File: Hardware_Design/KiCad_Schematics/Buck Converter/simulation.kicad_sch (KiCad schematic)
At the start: 8 parts, among them Q2 PMOS

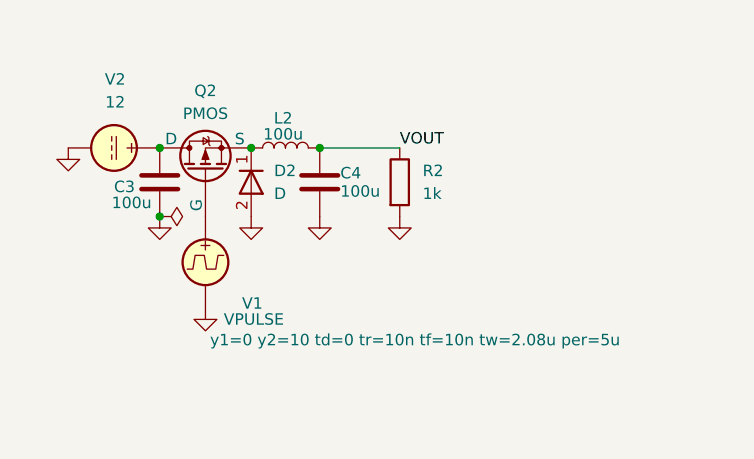
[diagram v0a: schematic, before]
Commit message: init: initialize new circuit for the previous problem
Started the Bootstrap Driver circuit to solve the previous problem. This way, the NMOSFET will be able to operate in full saturation.
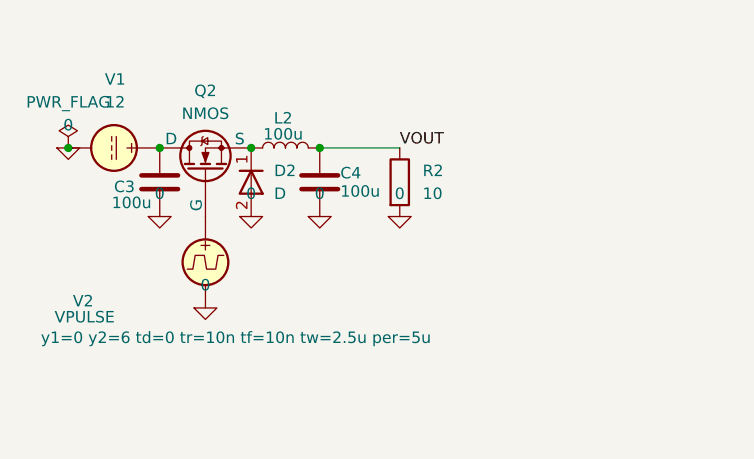
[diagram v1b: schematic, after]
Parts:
- removed Q2: PMOS, symbol Simulation_SPICE:PMOS
- added Q2: NMOS, symbol Simulation_SPICE:NMOS
- R2: value 1k -> 10
- renumbered V2 to V1, V1 to V2
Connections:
- net at C3.1, V1.1: now also Q2.1 (D)
- net at V2.1: now also Q2.2 (G)
- net at D2.1 (K), L2.1: now also Q2.3 (S)
- net GND renamed 0

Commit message: Update designs but continue problems...
Added a Bootstrap circuit to bring the MOSFET from a Linear Regulator state to a Buck Converter state, but the problem is still not resolved. While it should yield a value close to 6V when the Duty Cycle is at 50% and a 12V input is applied, it yields 4V, and the graph is not correct. Work on the problem will continue.
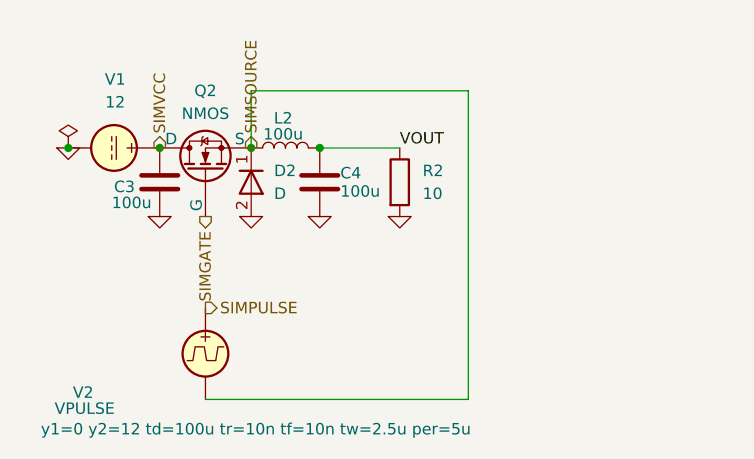
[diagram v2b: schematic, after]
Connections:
- net 0: no longer V2.2
- net SIMVCC: now reaches C3.1, Q2.1 (D), V1.1
- net SIMSOURCE: now reaches D2.1 (K), L2.1, Q2.3 (S)
- net SIMSOURCE: now also V2.2
- net SIMGATE: now reaches Q2.2 (G)
- net SIMGATE: no longer V2.1
- new net SIMPULSE: V2.1
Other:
- moved on the sheet: V2
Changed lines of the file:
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@@
+	(wire
+		(pts
+			(xy 151.13 85.09) (xy 127 85.09)
+		)
+		(stroke
+			(width 0)
+			(type default)
+		)
+	)
 	(wire
 		(pts
 			(xy 143.51 91.44) (xy 134.62 91.44)
+		)
+		(stroke
+			(width 0)
+			(type default)
+		)
+	)
+	(wire
+		(pts
+			(xy 127 85.09) (xy 127 91.44)
+		)
+		(stroke
+			(width 0)
+			(type default)
+		)
+	)
+	(wire
+		(pts
+			(xy 121.92 119.38) (xy 151.13 119.38)
+		)
+		(stroke
+			(width 0)
+			(type default)
+		)
+	)
+	(wire
+		(pts
+			(xy 151.13 119.38) (xy 151.13 85.09)
 		)
 		(stroke
@@
 		)
 	)
+	(hierarchical_label "SIMSOURCE"
+		(shape output)
+		(at 127 91.44 90)
+		(effects
+			(font
+				(size 1.27 1.27)
+			)
+			(justify left)
+		)
+	)
+	(hierarchical_label "SIMPULSE"
+		(shape output)
+		(at 121.92 109.22 0)
+		(effects
+			(font
+				(size 1.27 1.27)
+			)
+			(justify left)
+		)
+	)
+	(hierarchical_label "SIMVCC"
+		(shape output)
+		(at 116.84 91.44 90)
+		(effects
+			(font
+				(size 1.27 1.27)
+			)
+			(justify left)
+		)
+	)
+	(hierarchical_label "SIMGATE"
+		(shape output)
+		(at 121.92 99.06 270)
+		(effects
+			(font
+				(size 1.27 1.27)
+			)
+			(justify right)
+		)
+	)
 	(symbol
 		(lib_id "Device:C")
@@
 		(property "Value" "0"
 			(at 106.68 88.9 0)
+			(hide yes)
 			(show_name no)
 			(do_not_autoplace no)
@@
 	(symbol
 		(lib_id "Simulation_SPICE:VPULSE")
-		(at 121.92 104.14 0)
+		(at 121.92 114.3 0)
 		(unit 1)
 		(body_style 1)
@@
 		(dnp no)
 		(property "Reference" "V2"
-			(at 107.188 108.458 0)
+			(at 107.188 118.618 0)
 			(show_name no)
 			(do_not_autoplace no)
@@
 		)
 		(property "Value" "VPULSE"
-			(at 105.156 110.236 0)
+			(at 105.156 120.396 0)
 			(show_name no)
 			(do_not_autoplace no)
@@
 		)
 		(property "Footprint" ""
-			(at 121.92 104.14 0)
+			(at 121.92 114.3 0)
 			(hide yes)
 			(show_name no)
@@
 		)
 		(property "Datasheet" "https://ngspice.sourceforge.io/docs/ngspice-html-manual/manual.xhtml#sec_Independent_Sources_for"
-			(at 121.92 104.14 0)
+			(at 121.92 114.3 0)
 			(hide yes)
 			(show_name no)
@@
 		)
 		(property "Description" "Voltage source, pulse"
-			(at 121.92 104.14 0)
+			(at 121.92 114.3 0)
 			(hide yes)
 			(show_name no)
@@
 		)
 		(property "Sim.Pins" "1=+ 2=-"
-			(at 121.92 104.14 0)
+			(at 121.92 114.3 0)
 			(hide yes)
 			(show_name no)
@@
 		)
 		(property "Sim.Type" "PULSE"
-			(at 121.92 104.14 0)
+			(at 121.92 114.3 0)
 			(hide yes)
 			(show_name no)
@@
 		)
 		(property "Sim.Device" "V"
-			(at 121.92 104.14 0)
+			(at 121.92 114.3 0)
 			(hide yes)
 			(show_name no)
@@
 			)
 		)
-		(property "Sim.Params" "y1=0 y2=6 td=0 tr=10n tf=10n tw=2.5u per=5u"
-			(at 103.632 112.522 0)
+		(property "Sim.Params" "y1=0 y2=12 td=100u tr=10n tf=10n tw=2.5u per=5u"
+			(at 103.632 122.682 0)
 			(show_name no)
 			(do_not_autoplace no)
@@
 		(property "Value" "PWR_FLAG"
 			(at 106.68 86.36 0)
+			(hide yes)
 			(show_name no)
 			(do_not_autoplace no)
@@
 		(property "Value" "0"
 			(at 127 96.52 0)
+			(hide yes)
 			(show_name no)
 			(do_not_autoplace no)
@@
 		(property "Value" "0"
 			(at 143.51 96.52 0)
+			(hide yes)
 			(show_name no)
 			(do_not_autoplace no)
@@
 		(property "Value" "0"
 			(at 116.84 96.52 0)
+			(hide yes)
 			(show_name no)
 			(do_not_autoplace no)
@@
 	(symbol
 		(lib_id "Simulation_SPICE:0")
-		(at 121.92 109.22 0)
-		(unit 1)
-		(body_style 1)
-		(exclude_from_sim no)
-		(in_bom yes)
-		(on_board yes)
-		(in_pos_files yes)
-		(dnp no)
-		(fields_autoplaced yes)
-		(property "Reference" "#GND06"
-			(at 121.92 114.3 0)
-			(hide yes)
-			(show_name no)
-			(do_not_autoplace no)
-			(effects
-				(font
-					(size 1.27 1.27)
-				)
-			)
-		)
-		(property "Value" "0"
-			(at 121.92 106.68 0)
-			(show_name no)
-			(do_not_autoplace no)
-			(effects
-				(font
-					(size 1.27 1.27)
-				)
-			)
-		)
-		(property "Footprint" ""
-			(at 121.92 109.22 0)
-			(hide yes)
-			(show_name no)
-			(do_not_autoplace no)
-			(effects
-				(font
-					(size 1.27 1.27)
-				)
-			)
-		)
-		(property "Datasheet" "https://ngspice.sourceforge.io/docs/ngspice-html-manual/manual.xhtml#subsec_Circuit_elements__device"
-			(at 121.92 119.38 0)
-			(hide yes)
-			(show_name no)
-			(do_not_autoplace no)
-			(effects
-				(font
-					(size 1.27 1.27)
-				)
-			)
-		)
-		(property "Description" "0V reference potential for simulation"
-			(at 121.92 116.84 0)
-			(hide yes)
-			(show_name no)
-			(do_not_autoplace no)
-			(effects
-				(font
-					(size 1.27 1.27)
-				)
-			)
-		)
-		(pin "1"
-		)
-		(instances
-			(project "buck_converter"
-				(path "/e6ad1407-9765-4ff4-965d-dd4ca2472230/73cf55f2-6ad2-4256-9459-c6c839187002"
-					(reference "#GND06")
-					(unit 1)
-				)
-			)
-		)
-	)
-	(symbol
-		(lib_id "Simulation_SPICE:0")
 		(at 134.62 99.06 0)
 		(unit 1)
@@
 		(property "Value" "0"
 			(at 134.62 96.52 0)
-			(show_name no)
-			(do_not_autoplace no)
+			(hide yes)
+			(show_name no)
+			(do_not_autoplace no)
